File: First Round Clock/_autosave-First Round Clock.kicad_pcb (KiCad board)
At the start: 2 copper layers, 118 x 118 mm, 37 parts, among them J1 PJ-102AH, J2 Conn_01x06, J3 Conn_02x03_Odd_Even, SW1 Omron_B3F_SPST, SW2 Omron_B3F_SPST, SW3 Omron_B3F_SPST, SW4 Omron_B3F_SPST, U1 L7805, U2 ATmega328-PU, U3 DS1307_DIP-8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

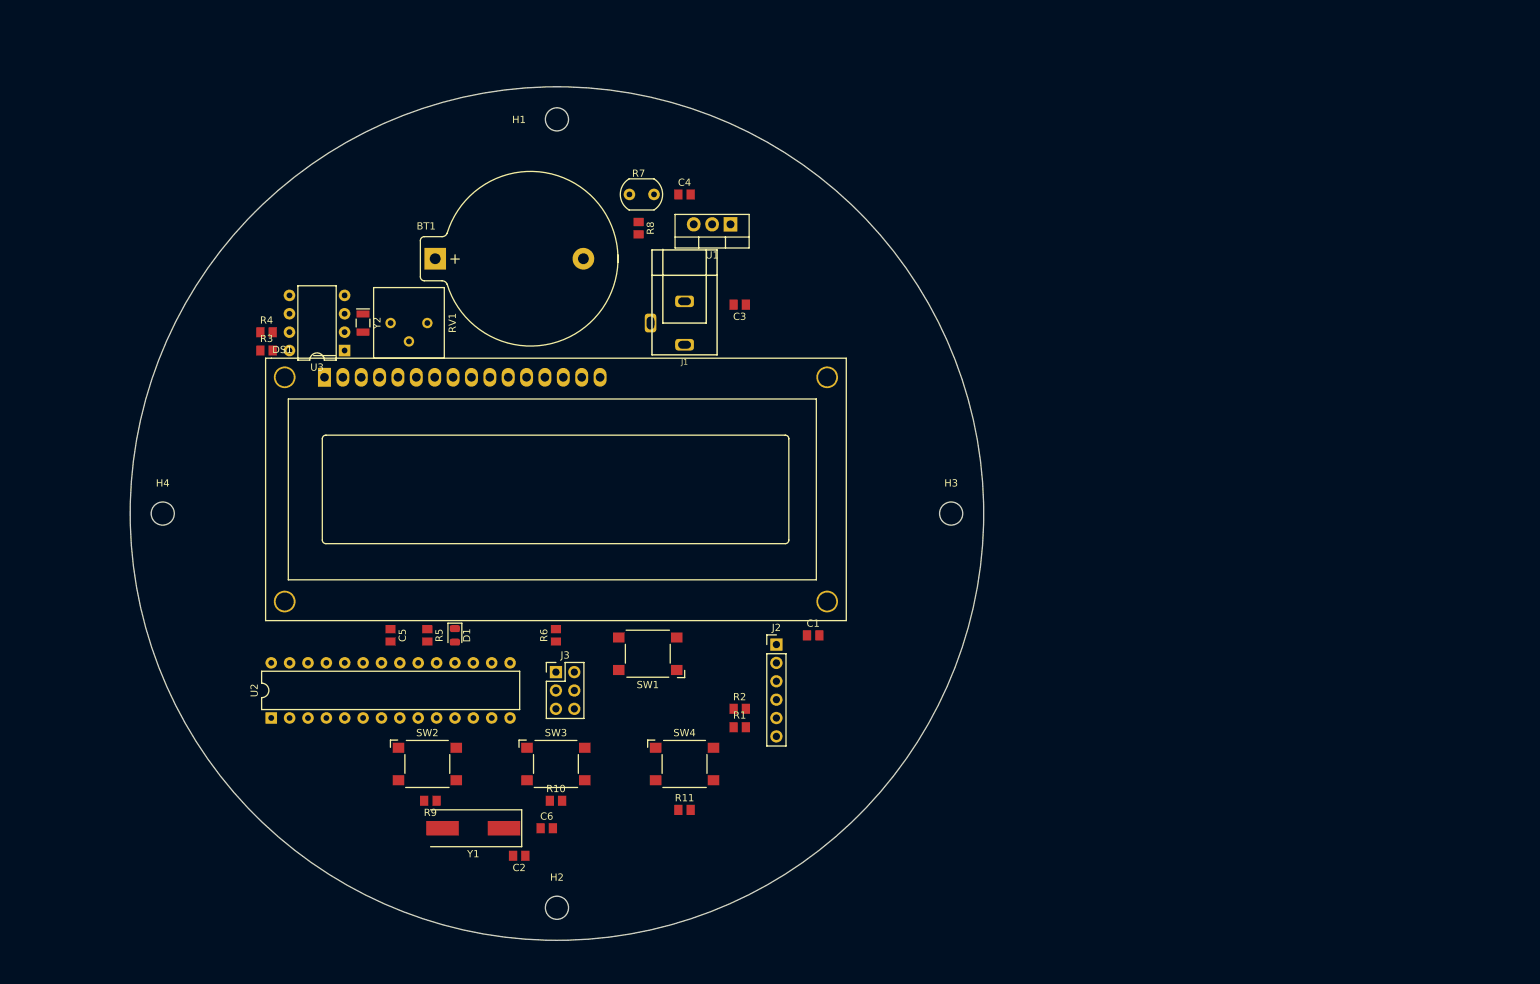
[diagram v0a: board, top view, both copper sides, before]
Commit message: Updated BOM and schematic
New and final BOM
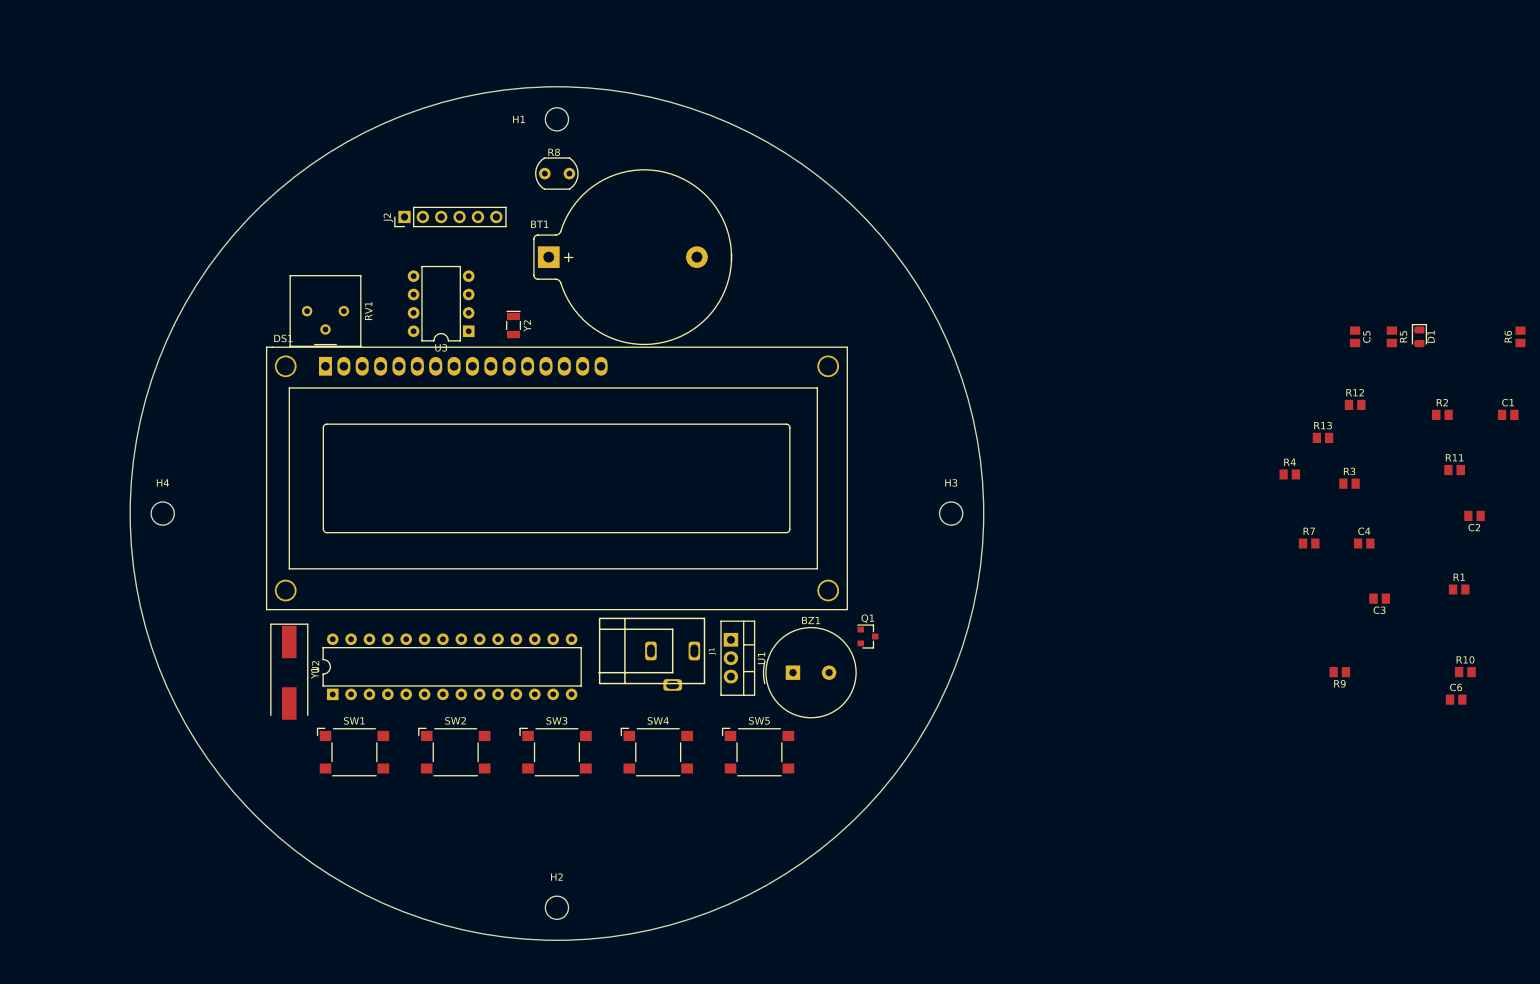
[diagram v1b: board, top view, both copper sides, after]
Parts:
- removed J3: Conn_02x03_Odd_Even, footprints:PinHeader_2x03_P2.54mm_Vertical
- added BZ1: Buzzer, footprints:Buzzer_TDK_PS1240P02BT_D12.2mm_H6.5mm, F.Cu at (182.6, 122.0)
- added Q1: NPN_2N3904_SOT23, footprints:SOT-23, F.Cu at (193.0, 117.0)
- added R12: R_0805_10K, footprints:R_0805_2012Metric, F.Cu at (260.4, 85.0)
- added R13: R_0805_10K, footprints:R_0805_2012Metric, F.Cu at (255.9, 89.5)
- added SW5: Omron_B3F_SPST, footprints:SW_SPST_Omron_B3FS-100xP, F.Cu at (178.0, 133.0)
- R7: value PhotoconductivePhotocell -> R_0805_2.2K; footprint footprints:R_LDR_4.9x4.2mm_P2.54mm_Vertical -> footprints:R_0805_2012Metric
- R8: value R_0805_100K -> PhotoconductivePhotocell; footprint footprints:R_0805_2012Metric -> footprints:R_LDR_4.9x4.2mm_P2.54mm_Vertical
- R9: value R_0805_10K -> R_0805_100K
- moved R3 150.8 mm to (259.6, 95.9)
- moved R4 142.8 mm to (251.3, 94.6)
- moved C2 140.2 mm to (276.9, 100.3)
- moved C5 139.6 mm to (260.4, 75.6)
- moved D1 139.6 mm to (269.2, 75.6)
- moved R5 139.6 mm to (265.4, 75.6)
- moved R6 139.6 mm to (283.2, 75.6)
- moved R9 127.0 mm to (258.2, 121.9)
- moved C6 127.0 mm to (274.3, 125.7)
- moved R10 127.0 mm to (275.6, 121.9)
- moved R11 116.4 mm to (274.1, 94.0)
- moved C4 105.6 mm to (261.6, 104.1)
- moved R7 105.6 mm to (254.0, 104.1)
- moved R2 105.3 mm to (272.4, 86.4)
- moved R1 101.3 mm to (274.7, 110.5)
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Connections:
- R10 pad 2: BTN_SELECT -> BTN_MODE
- R11 pad 2: BTN_UP -> BTN_DWN
- R7 pad 1: VCC -> Buzz
- R7 pad 2: LIGHT_SENSOR -> Net-(Q1-Pad1)
- R8 pad 1: LIGHT_SENSOR -> VCC
- R8 pad 2: GND -> LIGHT_SENSOR
- R9 pad 1: VCC -> LIGHT_SENSOR
- R9 pad 2: BTN_MODE -> GND
- SW3 pad 3: BTN_SELECT -> BTN_DWN
- SW3 pad 4: BTN_SELECT -> BTN_DWN
- SW4 pad 3: BTN_UP -> BTN_SELECT
- SW4 pad 4: BTN_UP -> BTN_SELECT
- U2 pad 17: MOSI -> unconnected-(U2-Pad17)
- U2 pad 18: MISO -> Buzz

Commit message: Week6
All deliverables for week 6
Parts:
- added AmOgUs: LOGO, LOGO, F.Cu at (102.4, 83.6)
- added G***: LOGO, footprints:HPS_logo, F.Cu at (174.0, 140.0)
- added J3: Conn_02x03_Odd_Even, footprints:PinHeader_2x03_P2.54mm_Vertical, F.Cu at (173.7, 116.5)
- added LeThs GoOoO: LOGO, LOGO, B.Cu at (113.3, 120.9)
- added R14: R_0805_10K, footprints:R_0805_2012Metric, F.Cu at (157.5, 124.0)
- BT1, BZ1, RV1: moved to B.Cu
- J1: value PJ-102AH -> Power_inlet_vertical; footprint footprints:PJ-102AH -> footprints:Wurth-694106402002; moved to B.Cu
- R10: value R_0805_10K -> R_0805_100K
- R5: value R_0805_2.2K -> R_0805_1K
- R6: value R_0805_10K -> R_0805_2.2K
- R7: value R_0805_2.2K -> R_0805_10K
- R8: value PhotoconductivePhotocell -> R_0805_1K; footprint footprints:R_LDR_4.9x4.2mm_P2.54mm_Vertical -> footprints:R_0805_2012Metric
- R9: value R_0805_100K -> PhotoconductivePhotocell; footprint footprints:R_0805_2012Metric -> footprints:R_LDR_4.9x4.2mm_P2.54mm_Vertical
- U1: footprint footprints:TO-220-3_Vertical -> footprints:TO-252-2
- moved R6 145.7 mm to (145.8, 124.0)
- moved R11 145.2 mm to (132.0, 124.0), turned to 90 degrees
- moved C6 140.4 mm to (135.0, 108.0), turned to -90 degrees
- moved D1 135.2 mm to (143.0, 124.0), turned to 90 degrees
- moved R9 126.4 mm to (151.7, 54.0)
- moved C3 126.2 mm to (142.0, 145.0), turned to 90 degrees
- moved R13 124.8 mm to (136.0, 124.0), turned to 90 degrees
- moved C2 124.2 mm to (153.0, 109.0), turned to -90 degrees
- moved C4 123.8 mm to (142.0, 136.0)
- moved C5 121.8 mm to (148.6, 124.0)
- moved C1 115.0 mm to (169.0, 110.0)
- moved R12 114.4 mm to (152.7, 123.7), turned to 90 degrees
- moved R2 113.9 mm to (161.0, 110.0)
- moved R10 113.6 mm to (162.0, 124.0), turned to -90 degrees
- moved R1 109.7 mm to (165.0, 110.0)
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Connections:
- R10 pad 1: VCC -> LIGHT_SENSOR
- R10 pad 2: BTN_MODE -> GND
- R11 pad 2: BTN_DWN -> BTN_MODE
- R12 pad 2: BTN_SELECT -> BTN_DWN
- R13 pad 2: BTN_UP -> BTN_SELECT
- R5 pad 1: Net-(D1-Pad1) -> VCC
- R5 pad 2: GND -> Net-(BZ1-Pad2)
- R6 pad 1: VCC -> Net-(D1-Pad1)
- R6 pad 2: RESET -> GND
- R7 pad 1: Buzz -> VCC
- R7 pad 2: Net-(Q1-Pad1) -> RESET
- R8 pad 1: VCC -> Buzz
- R8 pad 2: LIGHT_SENSOR -> Net-(Q1-Pad1)
- R9 pad 1: LIGHT_SENSOR -> VCC
- R9 pad 2: GND -> LIGHT_SENSOR
- U2 pad 11: LCD_11 -> LCD_12
- U2 pad 12: LCD_12 -> LCD_11
- U2 pad 13: LCD_13 -> LCD_6
- U2 pad 14: LCD_14 -> LCD_4
- U2 pad 15: LCD_4 -> BTN_MODE
- U2 pad 16: LCD_6 -> BTN_SELECT
- U2 pad 17: unconnected-(U2-Pad17) -> MOSI
- U2 pad 18: Buzz -> MISO
- U2 pad 23: Light_Sensor -> BTN_DWN
- U2 pad 24: unconnected-(U2-Pad24) -> BTN_UP
- U2 pad 26: unconnected-(U2-Pad26) -> LIGHT_SENSOR
- U2 pad 4: BTN_MODE -> Buzz
- U2 pad 5: BTN_SEL -> LCD_14
- U2 pad 6: BTN_UP -> LCD_13
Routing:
- net GND: track 0.00 -> 265.3 mm
- net SCL: track 0.00 -> 146.9 mm
- net SDA: track 0.00 -> 132.2 mm
- net LIGHT_SENSOR: track 0.00 -> 84.4 mm
- net LED_SCK: track 0.00 -> 64.6 mm
- net MOSI: track 0.00 -> 61.3 mm
- net BTN_DWN: track 0.00 -> 60.7 mm
- net BTN_UP: track 0.00 -> 57.6 mm
- net MISO: track 0.00 -> 52.4 mm
- net LCD_11: track 0.00 -> 51.4 mm
- net LCD_4: track 0.00 -> 50.0 mm
- net LCD_6: track 0.00 -> 46.8 mm
- net LCD_14: track 0.00 -> 46.1 mm
- net LCD_13: track 0.00 -> 44.1 mm
- net LCD_12: track 0.00 -> 43.0 mm
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- added copper zone on B.Cu, net GND
- added copper zone on F.Cu, net VCC
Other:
- board text added: "Andrew Perez's really cool and epic clock"
